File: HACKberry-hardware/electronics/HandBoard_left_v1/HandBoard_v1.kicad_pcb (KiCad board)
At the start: 2 copper layers, 60.8 x 54.8 mm, 12 parts, among them CON1 BARREL_JACK, SW1:MAX1 SW_PUSH_SKRGAQD010, SW2:MIN1 SW_PUSH_SKRGAQD010, SW3:Thumb1 SW_PUSH_SKRGAQD010, SW4:Middle1 SW_PUSH_SKRGAQD010, SW5 SWITCH_SS-12SDP2, U1 3-CONDUCTOR_MINIATUIRE_JACK_M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, U2 Arduino_Micro, U3 Seed_Studio_Adjustable_DC/DC_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, U4 Servo_Motor_S03N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

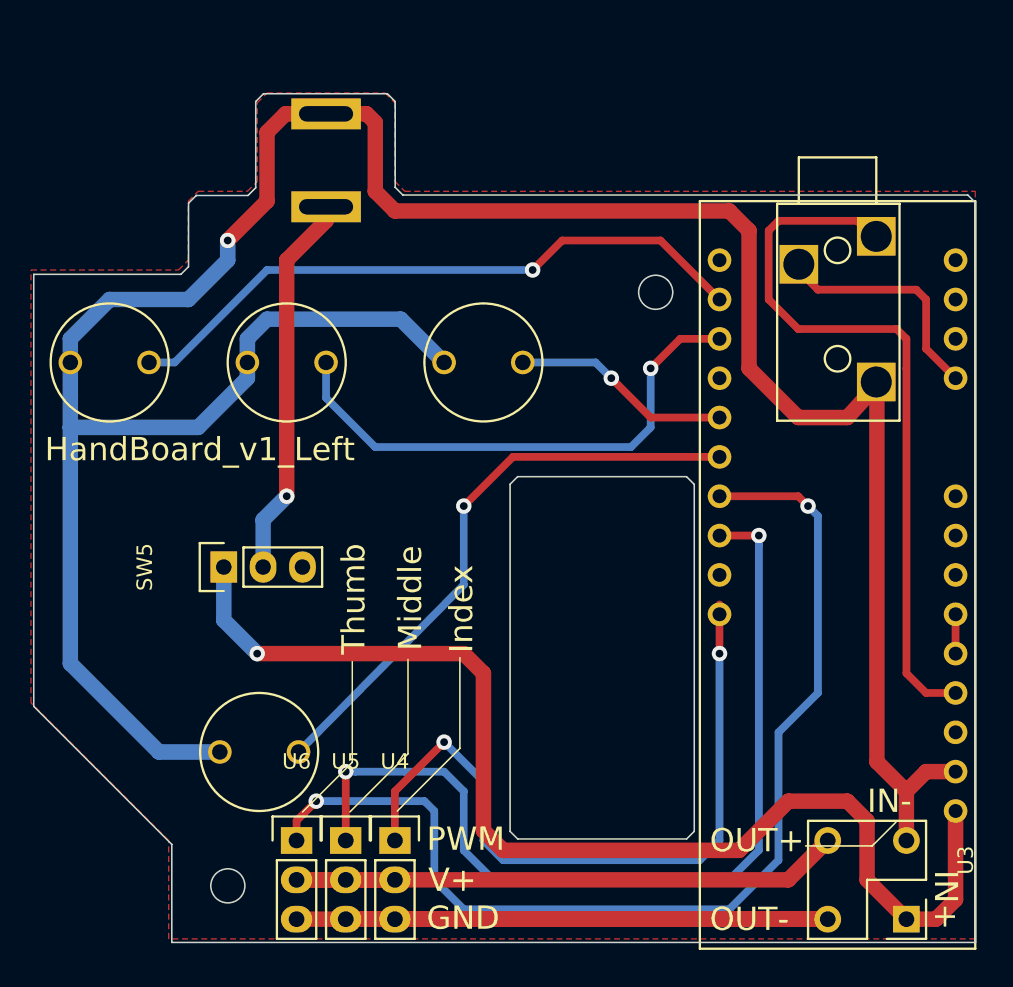
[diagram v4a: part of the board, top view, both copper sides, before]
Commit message: added drill for eyephone jack
added polygon for GND on buttom layer
made garbar data
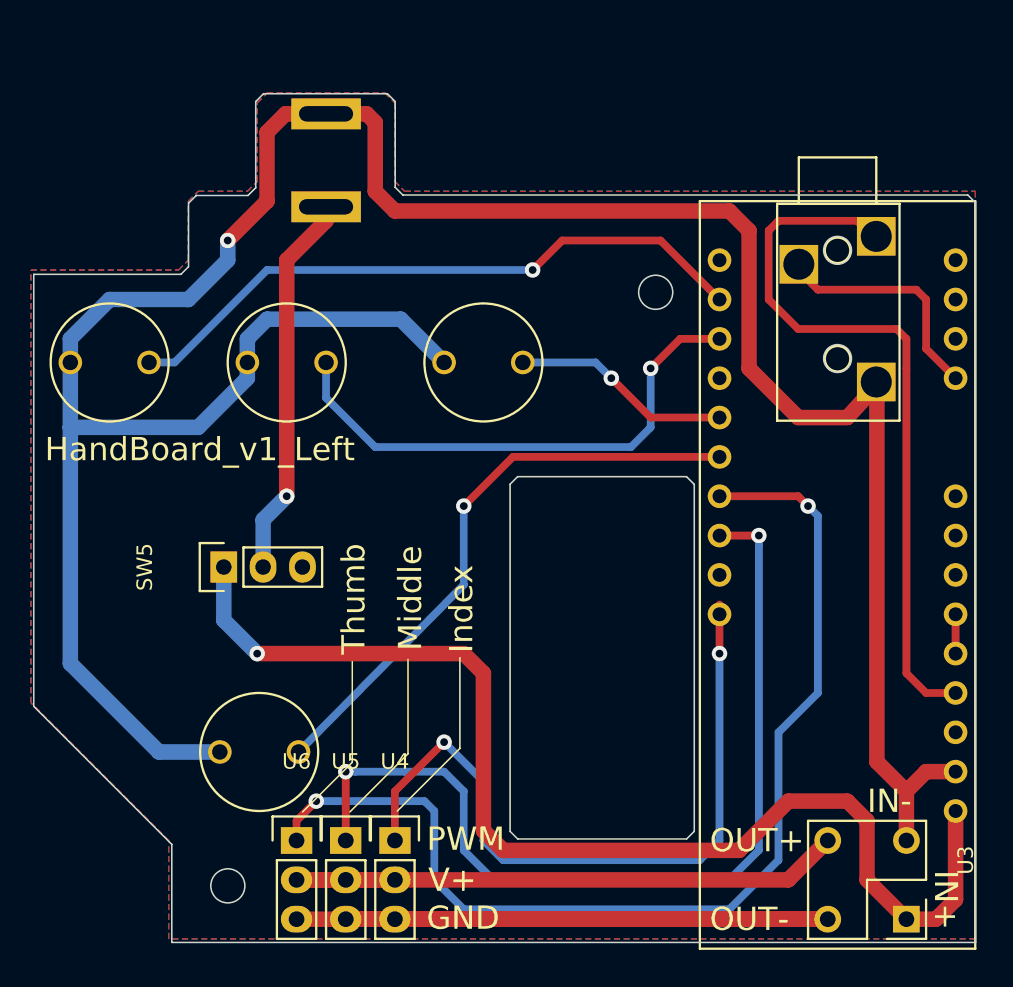
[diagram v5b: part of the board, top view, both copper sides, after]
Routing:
- added copper zone on B.Cu, net Net-(CON1-Pad2)
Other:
- outline, holes or cut-outs redrawn
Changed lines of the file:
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@@
   )
   (setup
-    (last_trace_width 1)
+    (last_trace_width 0.5)
     (user_trace_width 0.5)
     (user_trace_width 1)
@@
       (drillshape 0)
       (scaleselection 1)
-      (outputdirectory 160229HandBoard_v1_2/))
+      (outputdirectory 160615HandBoard_v1/))
   )
   (net 0 "")
@@
     (uvia_drill 0.1)
   )
+  (module HACKberry_v1:Pin_Header_Straight_2x02_Left_DCDC (layer F.Cu)
+    (at 151.6761 134.8486 270)
+    (descr "Through hole pin header")
+    (tags "pin header")
+    (fp_text reference U3 (at 0 -5.1 270) (layer F.SilkS)
+      (effects (font (size 1 1) (thickness 0.15)))
+    )
+    (fp_text value "Seed_Studio_Adjustable_DC/DC_Power_Converter_(1.25V_-_35V/3A)" (at 0 -3.81 270) (layer F.Fab)
+      (effects (font (size 1 1) (thickness 0.15)))
+    )
+    (fp_line (start 2.54 -2.54) (end 5.08 -2.54) (layer F.SilkS) (width 0.15))
+    (fp_line (start 5.08 -2.54) (end 5.08 0) (layer F.SilkS) (width 0.15))
+    (fp_line (start -2.54 -2.54) (end -2.54 5.08) (layer F.SilkS) (width 0.15))
+    (fp_line (start -2.54 5.08) (end 5.08 5.08) (layer F.SilkS) (width 0.15))
+    (fp_line (start 5.08 5.08) (end 5.08 1.27) (layer F.SilkS) (width 0.15))
+    (fp_line (start 5.08 1.27) (end 1.27 1.27) (layer F.SilkS) (width 0.15))
+    (fp_line (start 1.27 1.27) (end 1.27 -2.54) (layer F.SilkS) (width 0.15))
+    (fp_line (start 1.27 -2.54) (end -2.54 -2.54) (layer F.SilkS) (width 0.15))
+    (pad 1 thru_hole rect (at 3.81 -1.27 270) (size 1.7272 1.7272) (drill 1.016) (layers *.Cu *.Mask F.SilkS)
+      (net 2 "Net-(SW5-Pad1)"))
+    (pad 2 thru_hole oval (at -1.27 -1.27 270) (size 1.7272 1.7272) (drill 1.016) (layers *.Cu *.Mask F.SilkS)
+      (net 15 "Net-(CON1-Pad2)"))
+    (pad 3 thru_hole oval (at 3.81 3.81 270) (size 1.7272 1.7272) (drill 1.016) (layers *.Cu *.Mask F.SilkS)
+      (net 12 "Net-(U3-Pad3)"))
+    (pad 4 thru_hole oval (at -1.27 3.81 270) (size 1.7272 1.7272) (drill 1.016) (layers *.Cu *.Mask F.SilkS)
+      (net 13 "Net-(U3-Pad4)"))
+    (model Pin_Headers.3dshapes/Pin_Header_Straight_2x02.wrl
+      (at (xyz 0.05 -0.05 0))
+      (scale (xyz 1 1 1))
+      (rotate (xyz 0 0 90))
+    )
+  )
   (module HACKberry_v1:Arduino_Micro (layer F.Cu)
     (at 148.5011 116.4336 180)
@@
     )
   )
-  (module HACKberry_v1:Pin_Header_Straight_2x02_Left_DCDC (layer F.Cu)
-    (at 151.6761 134.8486 270)
-    (descr "Through hole pin header")
-    (tags "pin header")
-    (fp_text reference U3 (at 0 -5.1 270) (layer F.SilkS)
-      (effects (font (size 1 1) (thickness 0.15)))
-    )
-    (fp_text value "Seed_Studio_Adjustable_DC/DC_Power_Converter_(1.25V_-_35V/3A)" (at 0 -3.81 270) (layer F.Fab)
-      (effects (font (size 1 1) (thickness 0.15)))
-    )
-    (fp_line (start 2.54 -2.54) (end 5.08 -2.54) (layer F.SilkS) (width 0.15))
-    (fp_line (start 5.08 -2.54) (end 5.08 0) (layer F.SilkS) (width 0.15))
-    (fp_line (start -2.54 -2.54) (end -2.54 5.08) (layer F.SilkS) (width 0.15))
-    (fp_line (start -2.54 5.08) (end 5.08 5.08) (layer F.SilkS) (width 0.15))
-    (fp_line (start 5.08 5.08) (end 5.08 1.27) (layer F.SilkS) (width 0.15))
-    (fp_line (start 5.08 1.27) (end 1.27 1.27) (layer F.SilkS) (width 0.15))
-    (fp_line (start 1.27 1.27) (end 1.27 -2.54) (layer F.SilkS) (width 0.15))
-    (fp_line (start 1.27 -2.54) (end -2.54 -2.54) (layer F.SilkS) (width 0.15))
-    (pad 1 thru_hole rect (at 3.81 -1.27 270) (size 1.7272 1.7272) (drill 1.016) (layers *.Cu *.Mask F.SilkS)
-      (net 2 "Net-(SW5-Pad1)"))
-    (pad 2 thru_hole oval (at -1.27 -1.27 270) (size 1.7272 1.7272) (drill 1.016) (layers *.Cu *.Mask F.SilkS)
-      (net 15 "Net-(CON1-Pad2)"))
-    (pad 3 thru_hole oval (at 3.81 3.81 270) (size 1.7272 1.7272) (drill 1.016) (layers *.Cu *.Mask F.SilkS)
-      (net 12 "Net-(U3-Pad3)"))
-    (pad 4 thru_hole oval (at -1.27 3.81 270) (size 1.7272 1.7272) (drill 1.016) (layers *.Cu *.Mask F.SilkS)
-      (net 13 "Net-(U3-Pad4)"))
-    (model Pin_Headers.3dshapes/Pin_Header_Straight_2x02.wrl
-      (at (xyz 0.05 -0.05 0))
-      (scale (xyz 1 1 1))
-      (rotate (xyz 0 0 90))
-    )
-  )
   (module HACKberry_v1:MINIATURE_JACK_MJ-4535-3 (layer F.Cu)
     (at 148.5011 95.4786 90)
@@
       (net 15 "Net-(CON1-Pad2)"))
   )
+  (gr_circle (center 148.5011 102.4636) (end 149.1361 103.0986) (layer Edge.Cuts) (width 0.1))
+  (gr_circle (center 148.5011 95.4786) (end 149.1361 96.1136) (layer Edge.Cuts) (width 0.1))
   (gr_line (start 124.1211 127.6336) (end 124.1211 121.7836) (angle 90) (layer F.SilkS) (width 0.1))
   (gr_line (start 120.0711 131.6836) (end 124.1211 127.6336) (angle 90) (layer F.SilkS) (width 0.1))
@@
     (effects (font (size 1.5 1.5) (thickness 0.3)) (justify left))
   )
-  (gr_line (start 150.7371 133.9296) (end 152.2871 132.3796) (angle 90) (layer F.SilkS) (width 0.1))
-  (gr_line (start 146.4371 133.9296) (end 150.7371 133.9296) (angle 90) (layer F.SilkS) (width 0.1))
   (gr_text OUT- (at 140.2461 138.6586) (layer F.SilkS)
     (effects (font (size 1.5 1.5) (thickness 0.3)) (justify left))
@@
       )
     )
+  )
+  (zone (net 15) (net_name "Net-(CON1-Pad2)") (layer B.Cu) (hatch edge 0.508)
+    (connect_pads (clearance 0.508))
+    (min_thickness 0.254)
+    (fill yes (arc_segments 16) (thermal_gap 0.508) (thermal_bridge_width 0.508))
+    (polygon
+      (pts
+        (xy 119.9261 85.9536) (xy 119.9261 91.0336) (xy 120.5611 91.6686) (xy 157.3911 91.6686) (xy 157.3911 139.9286)
+        (xy 105.3211 139.9286) (xy 105.3211 133.5786) (xy 96.4311 124.6886) (xy 96.4311 96.7486) (xy 105.9561 96.7486)
+        (xy 106.5911 96.1136) (xy 106.5911 92.3036) (xy 107.2261 91.6686) (xy 110.4011 91.6686) (xy 111.0361 91.0336)
+        (xy 111.0361 85.9536) (xy 111.6711 85.3186) (xy 119.2911 85.3186) (xy 119.9261 85.9536)
+      )
+    )

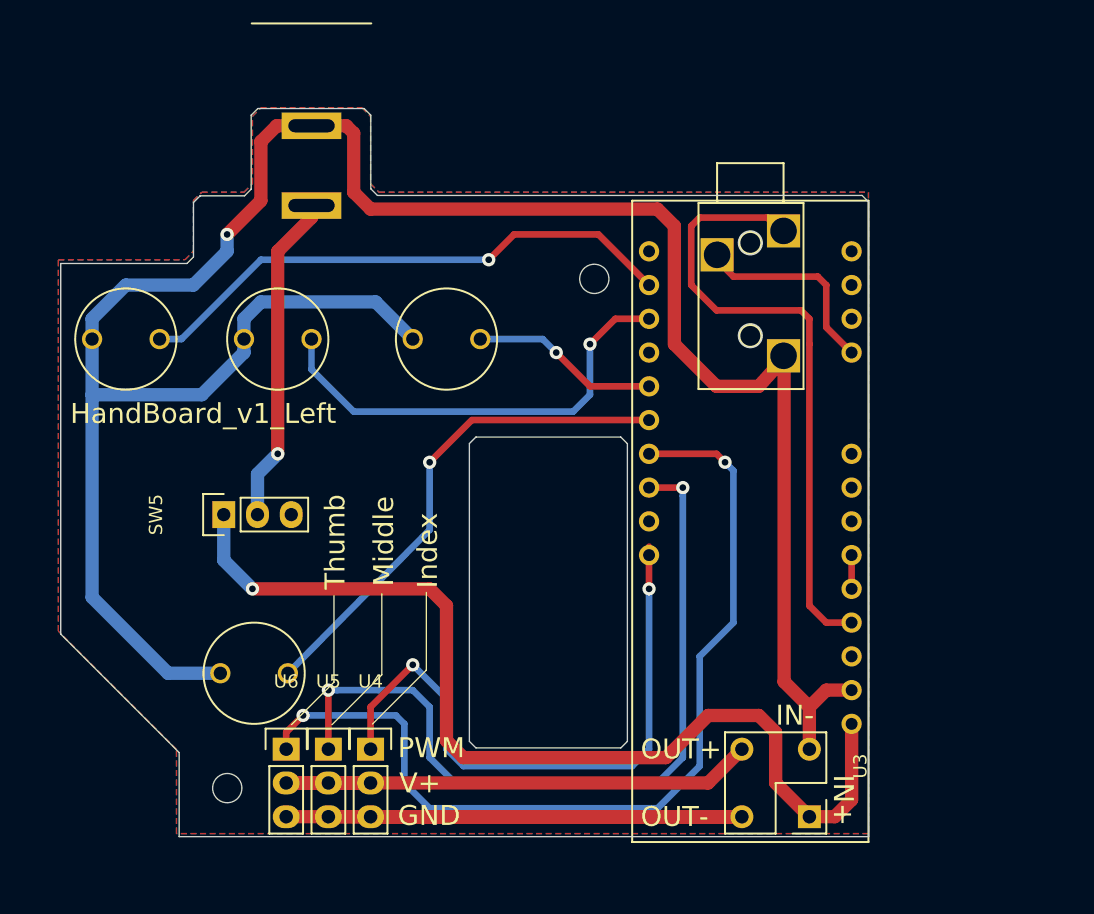
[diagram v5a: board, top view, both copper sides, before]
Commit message: Fix the positions of switches.
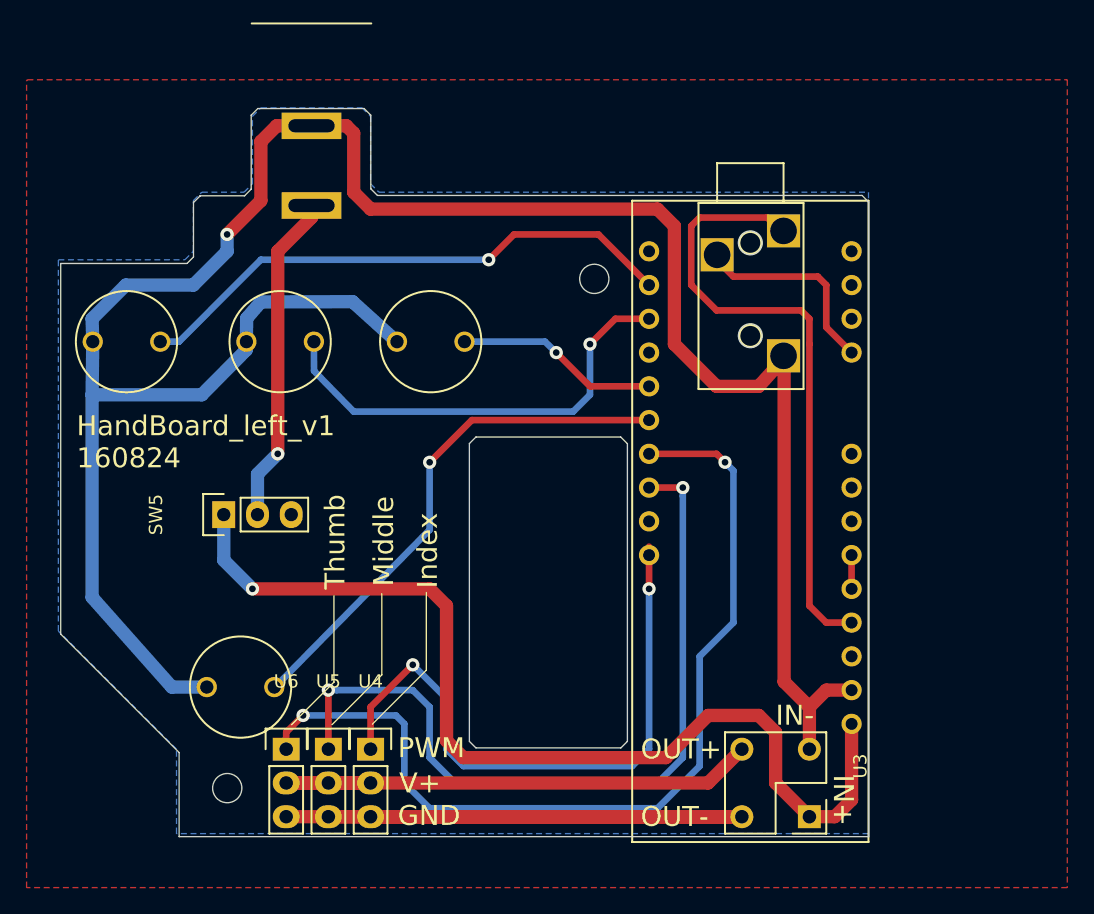
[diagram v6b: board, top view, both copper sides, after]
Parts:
- moved SW4:Middle1 1.46 mm to (110.1, 128.9)
- moved SW3:Thumb1 1.21 mm to (124.5, 102.9)
- moved SW2:MIN1 0.27 mm to (113.1, 102.9)
- moved SW1:MAX1 0.20 mm to (101.6, 102.9)
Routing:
- net Net-(CON1-Pad2): track 177.7 -> 176.1 mm
- net /SW_PINCH: track 38.1 -> 39.6 mm
- net /SW_MODE: track 14.2 -> 15.3 mm
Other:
- board text added: "HandBoard_left_v1 160824"
- board text removed: "HandBoard_v1_Left"
